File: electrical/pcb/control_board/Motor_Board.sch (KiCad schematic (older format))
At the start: 86 parts, among them J1 ED2627-ND, J11 S7038-ND_regulator_D24V22F12, J12 PPTC102LFBN-RC, J13 XT60-F, J14 ED2989-ND-USB, J15 XT60-F, J16 XT60-F, J17 Molex_172675-0613, J18 Molex_172675-0613, J19 Molex_172675-0613, J2 ED2627-ND, J20 Molex_172675-0613, J21 Molex_172675-0613, J22 Molex_172675-0613, J28 XT60-F, J29 XT60-F, J3 ED2627-ND, J30 XT60-F, J53 PEC08SAAN, J69 PEC04SAAN_5v_regulator_2, M1 Mounting_Holes, T1 test_point, T2 test_point, T3 test_point, T5 test_point, T6 test_point, y1 rover_silkscreen

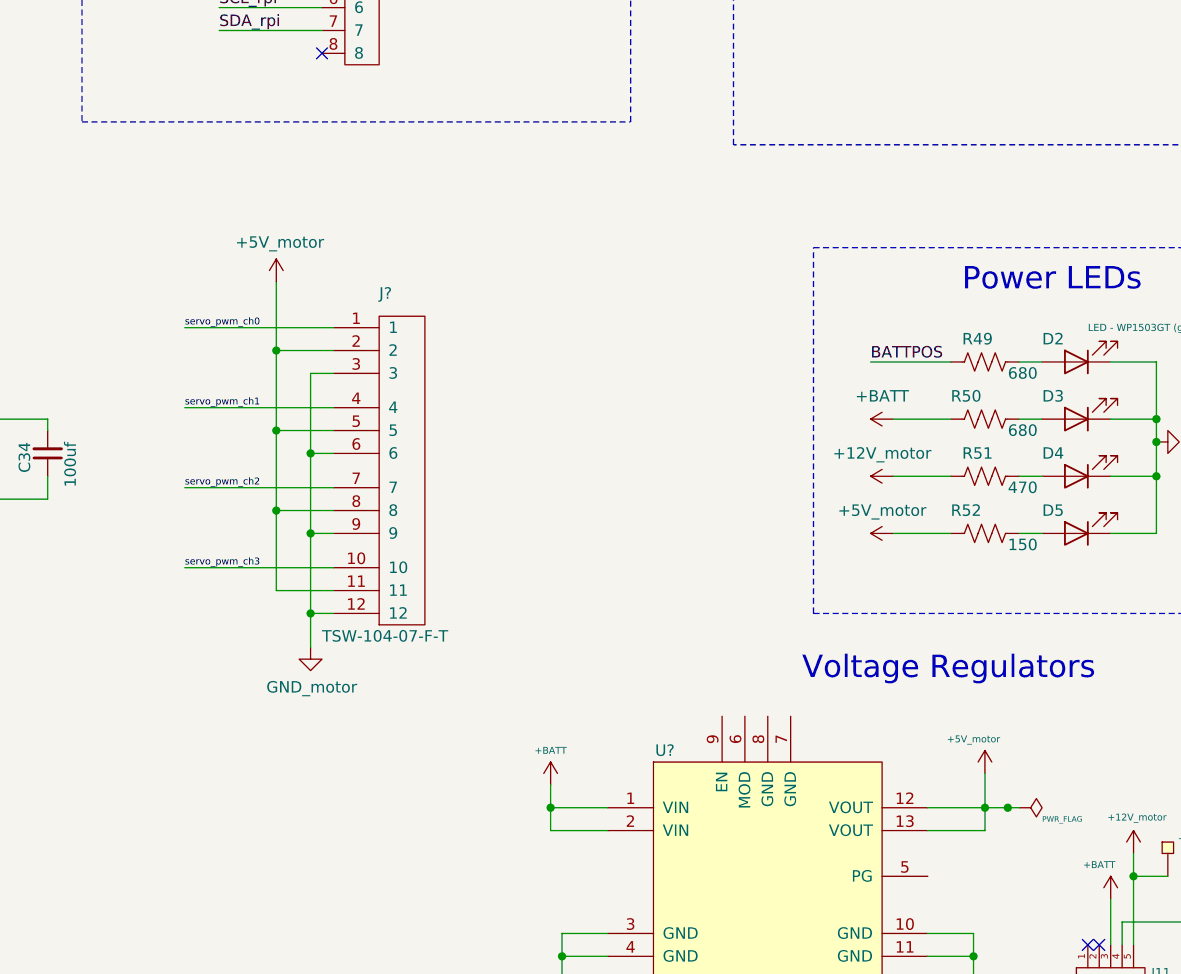
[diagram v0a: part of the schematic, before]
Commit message: Adding shcematic symbol for 4 pin molex connector, and adding to schematic
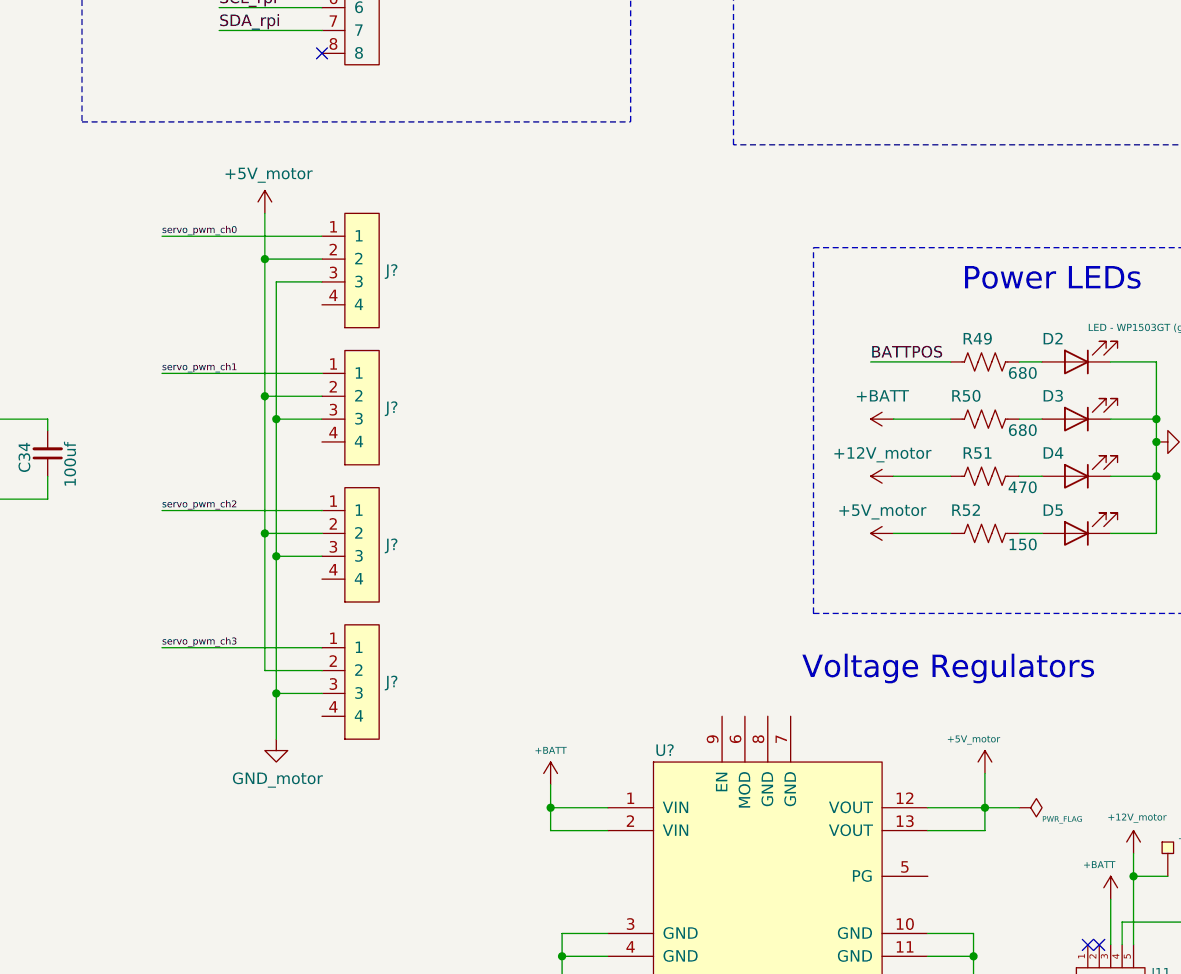
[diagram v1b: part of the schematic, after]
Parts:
- removed J?: TSW-104-07-F-T, symbol JPL_Robotics_Lib:TSW-104-07-F-T
- added J? (x4): 1726750413, symbol JPL_Robotics_Lib:1726750413
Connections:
- net +5V_motor: now also J?.2, J?.2, J?.2, J?.2
- net GND_motor: now also J?.3, J?.3, J?.3, J?.3
- net servo_pwm_ch0: now also J?.1
- net servo_pwm_ch1: now also J?.1
- net servo_pwm_ch2: now also J?.1
- net servo_pwm_ch3: now also J?.1
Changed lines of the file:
@@
 Text Notes 8200 7500 0    31   ~ 0
 I think these are staying unconnected
-$Comp
-L JPL_Robotics_Lib:TSW-104-07-F-T J?
-U 1 1 632C8AD7
-P 11600 7050
-F 0 "J?" H 11600 8600 50  0000 L CNN
-F 1 "TSW-104-07-F-T" H 11350 7100 50  0000 L CNN
-F 2 "" H 11600 7050 50  0001 C CNN
-F 3 "" H 11600 7050 50  0001 C CNN
-	1    11600 7050
-	1    0    0    -1
-$EndComp
-Text Label 10750 5650 0    30   ~ 0
+Text Label 10650 5250 0    30   ~ 0
 servo_pwm_ch0
-Text Label 10750 6000 0    30   ~ 0
+Text Label 10650 5850 0    30   ~ 0
 servo_pwm_ch1
-Text Label 10750 6350 0    30   ~ 0
+Text Label 10650 6450 0    30   ~ 0
 servo_pwm_ch2
-Text Label 10750 6700 0    30   ~ 0
+Text Label 10650 7050 0    30   ~ 0
 servo_pwm_ch3
 $Comp
 L JPL_Robotics_Lib:GND_motor #PWR?
 U 1 1 6350BD3C
-P 11300 7050
-F 0 "#PWR?" H 11300 6800 50  0001 C CNN
-F 1 "GND_motor" H 11305 6877 50  0000 C CNN
-F 2 "" H 11300 7050 50  0001 C CNN
-F 3 "" H 11300 7050 50  0001 C CNN
-	1    11300 7050
-	1    0    0    -1
-$EndComp
-Wire Wire Line
-	11400 6900 11300 6900
-Wire Wire Line
-	10750 6700 11400 6700
-Wire Wire Line
-	10750 6350 11400 6350
-Wire Wire Line
-	10750 6000 11400 6000
-Wire Wire Line
-	11300 6900 11300 6550
-Wire Wire Line
-	11300 6550 11400 6550
-Wire Wire Line
-	11300 6550 11300 6200
-Wire Wire Line
-	11300 6200 11400 6200
-Connection ~ 11300 6550
-Wire Wire Line
-	11300 6200 11300 5850
-Wire Wire Line
-	11300 5850 11400 5850
-Connection ~ 11300 6200
-Connection ~ 11300 6900
-Wire Wire Line
-	11300 6900 11300 7050
-Wire Wire Line
-	10750 5650 11400 5650
+P 11150 7450
+F 0 "#PWR?" H 11150 7200 50  0001 C CNN
+F 1 "GND_motor" H 11155 7277 50  0000 C CNN
+F 2 "" H 11150 7450 50  0001 C CNN
+F 3 "" H 11150 7450 50  0001 C CNN
+	1    11150 7450
+	1    0    0    -1
+$EndComp
 Wire Wire Line
 	9100 6300 9100 6400
@@
 L JPL_Robotics_Lib:+5V_motor #PWR?
 U 1 1 63D2C59E
-P 11150 5450
-F 0 "#PWR?" H 11150 5300 50  0001 C CNN
-F 1 "+5V_motor" H 11165 5623 50  0000 C CNN
-F 2 "" H 11150 5450 50  0001 C CNN
-F 3 "" H 11150 5450 50  0001 C CNN
-	1    11150 5450
-	1    0    0    -1
-$EndComp
-Wire Wire Line
-	11400 5750 11150 5750
-Wire Wire Line
-	11150 5750 11150 5450
-Wire Wire Line
-	11150 5750 11150 6100
-Wire Wire Line
-	11150 6100 11400 6100
-Connection ~ 11150 5750
-Wire Wire Line
-	11150 6100 11150 6450
-Wire Wire Line
-	11150 6450 11400 6450
-Connection ~ 11150 6100
-Wire Wire Line
-	11150 6450 11150 6800
-Wire Wire Line
-	11150 6800 11400 6800
-Connection ~ 11150 6450
+P 11100 5150
+F 0 "#PWR?" H 11100 5000 50  0001 C CNN
+F 1 "+5V_motor" H 11115 5323 50  0000 C CNN
+F 2 "" H 11100 5150 50  0001 C CNN
+F 3 "" H 11100 5150 50  0001 C CNN
+	1    11100 5150
+	1    0    0    -1
+$EndComp
 $Comp
 L JPL_Robotics_Lib:TSW-104-07-F-T J?
@@
 Connection ~ 14250 7750
 Wire Wire Line
-	14400 7750 14350 7750
-Connection ~ 14350 7750
-Wire Wire Line
-	14350 7750 14250 7750
+	14250 7750 14400 7750
+$Comp
+L JPL_Robotics_Lib:1726750413 J?
+U 1 1 61D6004E
+P 11300 5650
+F 0 "J?" H 11628 5900 50  0000 L CNN
+F 1 "1726750413" H 11700 5600 50  0001 C CNN
+F 2 "" H 11450 6200 50  0001 C CNN
+F 3 "" H 11450 6200 50  0001 C CNN
+	1    11300 5650
+	1    0    0    -1
+$EndComp
+$Comp
+L JPL_Robotics_Lib:1726750413 J?
+U 1 1 61D6018B
+P 11300 6250
+F 0 "J?" H 11628 6500 50  0000 L CNN
+F 1 "1726750413" H 11700 6200 50  0001 C CNN
+F 2 "" H 11450 6800 50  0001 C CNN
+F 3 "" H 11450 6800 50  0001 C CNN
+	1    11300 6250
+	1    0    0    -1
+$EndComp
+$Comp
+L JPL_Robotics_Lib:1726750413 J?
+U 1 1 61D60397
+P 11300 6850
+F 0 "J?" H 11628 7100 50  0000 L CNN
+F 1 "1726750413" H 11700 6800 50  0001 C CNN
+F 2 "" H 11450 7400 50  0001 C CNN
+F 3 "" H 11450 7400 50  0001 C CNN
+	1    11300 6850
+	1    0    0    -1
+$EndComp
+$Comp
+L JPL_Robotics_Lib:1726750413 J?
+U 1 1 61D60475
+P 11300 7450
+F 0 "J?" H 11628 7700 50  0000 L CNN
+F 1 "1726750413" H 11700 7400 50  0001 C CNN
+F 2 "" H 11450 8000 50  0001 C CNN
+F 3 "" H 11450 8000 50  0001 C CNN
+	1    11300 7450
+	1    0    0    -1
+$EndComp
+Wire Wire Line
+	10650 7050 11350 7050
+Wire Wire Line
+	10650 6450 11350 6450
+Wire Wire Line
+	10650 5850 11350 5850
+Wire Wire Line
+	10650 5250 11350 5250
+Wire Wire Line
+	11100 5150 11100 5350
+Wire Wire Line
+	11100 5350 11350 5350
+Wire Wire Line
+	11100 5350 11100 5950
+Wire Wire Line
+	11100 5950 11350 5950
+Connection ~ 11100 5350
+Wire Wire Line
+	11100 5950 11100 6550
+Wire Wire Line
+	11100 6550 11350 6550
+Connection ~ 11100 5950
+Wire Wire Line
+	11100 6550 11100 7150
+Wire Wire Line
+	11100 7150 11350 7150
+Connection ~ 11100 6550
+Wire Wire Line
+	11150 7450 11150 7250
+Wire Wire Line
+	11150 7250 11350 7250
+Wire Wire Line
+	11150 7250 11150 6650
+Wire Wire Line
+	11150 6650 11350 6650
+Connection ~ 11150 7250
+Wire Wire Line
+	11150 6650 11150 6050
+Wire Wire Line
+	11150 6050 11350 6050
+Connection ~ 11150 6650
+Wire Wire Line
+	11150 6050 11150 5450
+Wire Wire Line
+	11150 5450 11350 5450
+Connection ~ 11150 6050
 $EndSCHEMATC
